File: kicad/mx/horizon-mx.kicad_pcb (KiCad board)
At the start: 2 copper layers, 266 x 76 mm, 117 parts, among them SW1 SW_Push, SW10 SW_Push, SW11 SW_Push, SW12 SW_Push, SW13 SW_Push, SW14 SW_Push, SW15 SW_Push, SW16 SW_Push, SW17 SW_Push, SW18 SW_Push, SW19 SW_Push, SW2 SW_Push, SW20 SW_Push, SW21 SW_Push, SW22 SW_Push, SW23 SW_Push, SW24 SW_Push, SW25 SW_Push, SW26 SW_Push, SW27 SW_Push, SW28 SW_Push, SW29 SW_Push, SW3 SW_Push, SW30 SW_Push, SW31 SW_Push, SW32 SW_Push, SW33 SW_Push, SW34 SW_Push, SW35 SW_Push, SW36 SW_Push, SW37 SW_Push, SW38 SW_Push, SW39 SW_Push, SW4 SW_Push, SW40 SW_Push, SW41 SW_Push, SW42 SW_Push, SW43 SW_Push, SW44 SW_Push, SW45 SW_Push, SW46 SW_Push, SW47 SW_Push, SW48 SW_Push, SW49 SW_Push, SW5 SW_Push, SW50 SW_Push, SW51 SW_Push, SW52 SW_Push, SW6 SW_Push, SW7 SW_Push, SW8 SW_Push, SW9 SW_Push, U1 PRO-MICRO

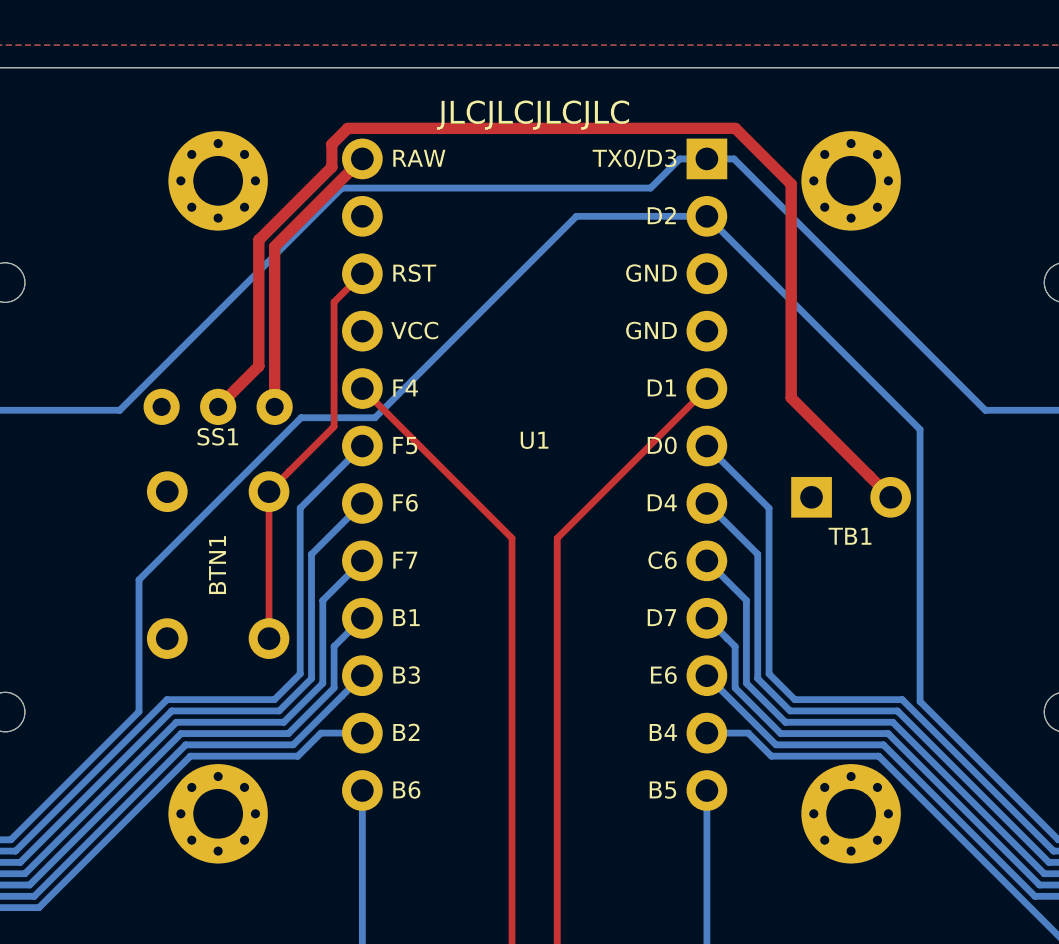
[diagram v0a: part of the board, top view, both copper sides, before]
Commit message: Clean up plate cuts, update MX board with battery removed
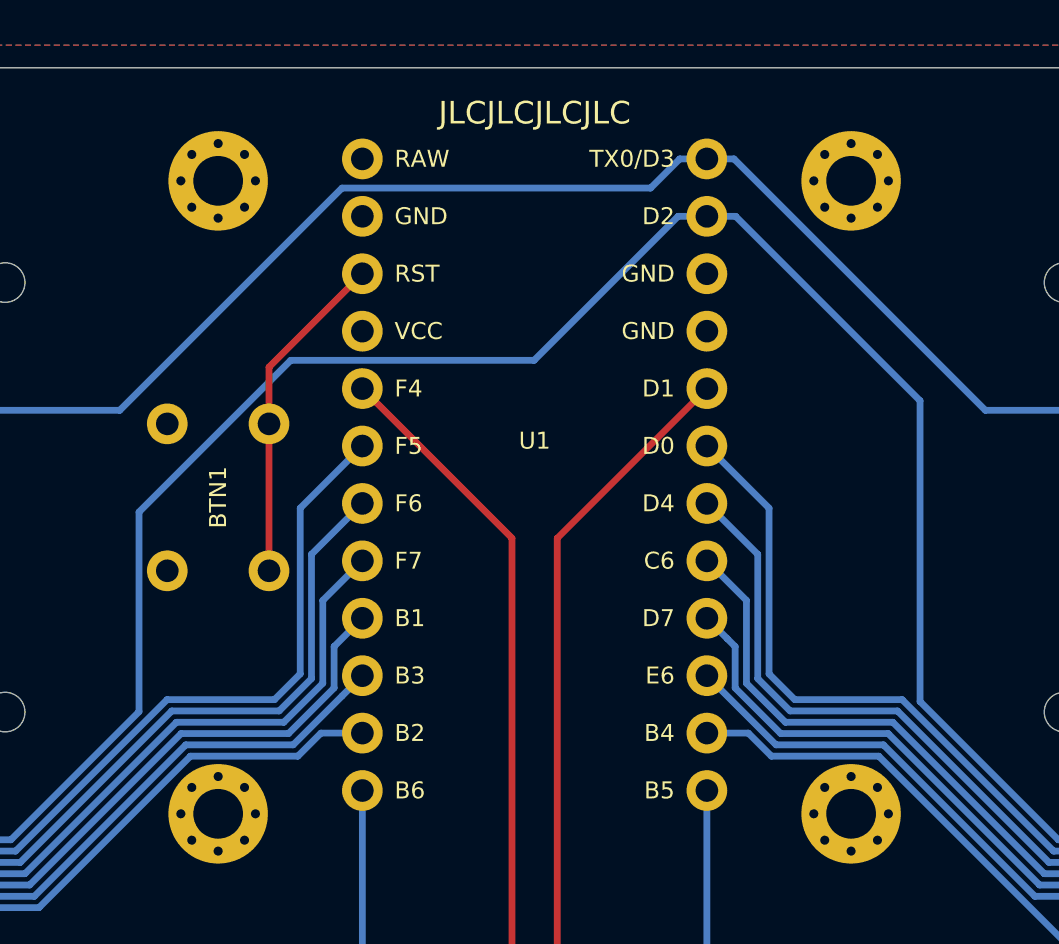
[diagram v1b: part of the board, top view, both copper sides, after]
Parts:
- removed SS1: POWER, horizon-footprints:SS12D00
- removed TB1: BATTERY, horizon-footprints:KF350-2P
- moved BTN1 3.00 mm to (195.0, 114.0)
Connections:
- U1 pad 24: RAW -> (no net)
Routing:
- net +BATT: track 51.0 -> 0.00 mm
- net RAW: track 12.6 -> 0.00 mm
- net RESET: track 17.9 -> 14.9 mm
- net ROW2: track 302.0 -> 304.5 mm

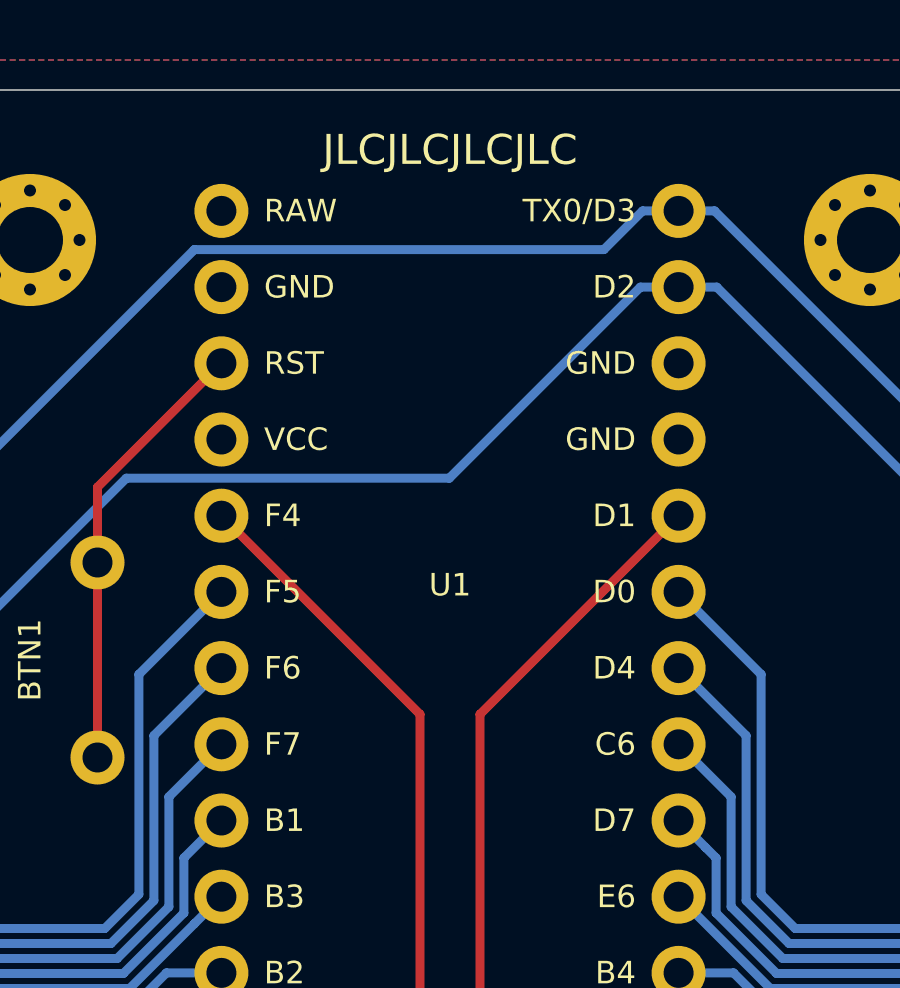
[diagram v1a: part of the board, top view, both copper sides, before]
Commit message: Preserve logos on plate PCBs
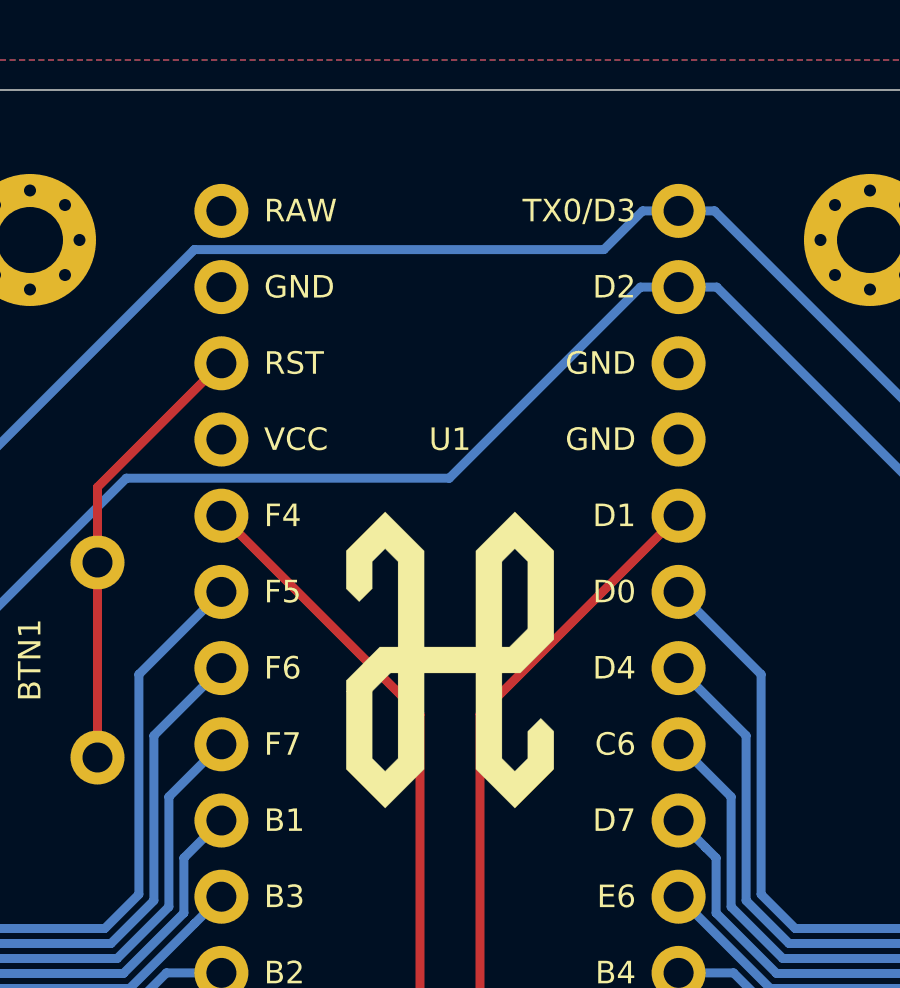
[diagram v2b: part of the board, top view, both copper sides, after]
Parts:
- added LOGO2: Logo-Top, horizon-footprints:Logo_Horizon_H, F.Cu at (209.0, 114.0)
- LOGO1: value Logo -> Logo-Bottom
- moved LOGO1 23.0 mm to (209.0, 100.5)
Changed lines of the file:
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@@
     (tracks 394)
     (zones 0)
-    (modules 115)
+    (modules 116)
     (nets 81)
   )
@@
     (add_net GND)
   )
+  (module horizon-footprints:Logo_Horizon_H (layer F.Cu)
+    (at 209 114)
+    (fp_text reference LOGO2 (at 0 2) (layer F.SilkS) hide
+      (effects (font (size 1.524 1.524) (thickness 0.3)))
+    )
+    (fp_text value Logo-Top (at 0 -2) (layer F.SilkS) hide
+      (effects (font (size 1.524 1.524) (thickness 0.3)))
+    )
+    (fp_poly (pts (xy 2.811161 -4.287795) (xy 3.459892 -3.639066) (xy 3.459892 -0.685799) (xy 2.900748 -0.126656)
+      (xy 2.341604 0.432486) (xy 1.731319 0.432486) (xy 1.731319 3.280722) (xy 1.94722 3.49662)
+      (xy 2.163122 3.712519) (xy 2.37902 3.496617) (xy 2.594919 3.280715) (xy 2.594919 2.378679)
+      (xy 2.810817 2.162777) (xy 2.83116 2.14244) (xy 2.850995 2.122623) (xy 2.870235 2.103411)
+      (xy 2.888793 2.084893) (xy 2.906579 2.067156) (xy 2.923508 2.050287) (xy 2.93949 2.034374)
+      (xy 2.954438 2.019503) (xy 2.968264 2.005761) (xy 2.980881 1.993237) (xy 2.9922 1.982017)
+      (xy 3.002134 1.972189) (xy 3.010594 1.96384) (xy 3.017494 1.957056) (xy 3.022745 1.951926)
+      (xy 3.02626 1.948537) (xy 3.02795 1.946975) (xy 3.028092 1.946875) (xy 3.029178 1.947832)
+      (xy 3.032118 1.950645) (xy 3.036821 1.955226) (xy 3.043201 1.961488) (xy 3.051169 1.969343)
+      (xy 3.060638 1.978705) (xy 3.07152 1.989485) (xy 3.083726 2.001596) (xy 3.097169 2.014952)
+      (xy 3.111761 2.029464) (xy 3.127413 2.045045) (xy 3.144038 2.061608) (xy 3.161548 2.079065)
+      (xy 3.179855 2.097329) (xy 3.198872 2.116313) (xy 3.218509 2.135929) (xy 3.238679 2.15609)
+      (xy 3.24468 2.162091) (xy 3.459892 2.377306) (xy 3.459892 3.639066) (xy 2.16243 4.936524)
+      (xy 1.513702 4.287791) (xy 0.864973 3.639058) (xy 0.864973 0.432486) (xy -0.8636 0.432486)
+      (xy -0.8636 3.639058) (xy -1.511985 4.287448) (xy -1.547393 4.322855) (xy -1.582321 4.357781)
+      (xy -1.616719 4.392174) (xy -1.650537 4.425985) (xy -1.683724 4.459163) (xy -1.716229 4.491659)
+      (xy -1.748003 4.52342) (xy -1.778995 4.554399) (xy -1.809155 4.584543) (xy -1.838431 4.613803)
+      (xy -1.866775 4.642128) (xy -1.894136 4.669469) (xy -1.920462 4.695774) (xy -1.945705 4.720994)
+      (xy -1.969813 4.745078) (xy -1.992736 4.767976) (xy -2.014425 4.789637) (xy -2.034827 4.810012)
+      (xy -2.053894 4.82905) (xy -2.071574 4.8467) (xy -2.087818 4.862913) (xy -2.102575 4.877638)
+      (xy -2.115795 4.890825) (xy -2.127427 4.902423) (xy -2.13742 4.912383) (xy -2.145726 4.920653)
+      (xy -2.152293 4.927184) (xy -2.15707 4.931925) (xy -2.160008 4.934826) (xy -2.161057 4.935837)
+      (xy -2.161058 4.935838) (xy -2.162058 4.934875) (xy -2.16495 4.932021) (xy -2.169682 4.927325)
+      (xy -2.176204 4.920839) (xy -2.184467 4.912612) (xy -2.194419 4.902694) (xy -2.20601 4.891136)
+      (xy -2.21919 4.877989) (xy -2.233909 4.863302) (xy -2.250116 4.847126) (xy -2.267761 4.829511)
+      (xy -2.286794 4.810508) (xy -2.307164 4.790166) (xy -2.32882 4.768536) (xy -2.351713 4.745669)
+      (xy -2.375792 4.721614) (xy -2.401007 4.696422) (xy -2.427307 4.670144) (xy -2.454642 4.642829)
+      (xy -2.482962 4.614527) (xy -2.512216 4.585291) (xy -2.542354 4.555168) (xy -2.573326 4.52421)
+      (xy -2.605081 4.492468) (xy -2.637569 4.45999) (xy -2.670739 4.426829) (xy -2.704541 4.393033)
+      (xy -2.738926 4.358654) (xy -2.773842 4.323741) (xy -2.810133 4.28745) (xy -3.458519 3.639063)
+      (xy -3.458519 1.044143) (xy -2.593546 1.044143) (xy -2.593546 3.280715) (xy -2.377648 3.496617)
+      (xy -2.161749 3.712519) (xy -1.945848 3.49662) (xy -1.729946 3.280722) (xy -1.729946 0.432486)
+      (xy -1.981884 0.432486) (xy -2.287715 0.738315) (xy -2.593546 1.044143) (xy -3.458519 1.044143)
+      (xy -3.458519 0.685798) (xy -2.899375 0.126656) (xy -2.340231 -0.432487) (xy -1.729946 -0.432487)
+      (xy -1.729946 -3.280722) (xy -1.945848 -3.496621) (xy -2.161749 -3.712519) (xy -2.377648 -3.496618)
+      (xy -2.593546 -3.280716) (xy -2.593546 -2.378679) (xy -2.809445 -2.162778) (xy -2.829787 -2.142441)
+      (xy -2.849622 -2.122623) (xy -2.868863 -2.103412) (xy -2.88742 -2.084894) (xy -2.905207 -2.067157)
+      (xy -2.922135 -2.050288) (xy -2.938117 -2.034374) (xy -2.953065 -2.019503) (xy -2.966892 -2.005762)
+      (xy -2.979508 -1.993238) (xy -2.990827 -1.982018) (xy -3.000761 -1.97219) (xy -3.009222 -1.96384)
+      (xy -3.016122 -1.957057) (xy -3.021373 -1.951927) (xy -3.024887 -1.948537) (xy -3.026578 -1.946975)
+      (xy -3.026719 -1.946876) (xy -3.027806 -1.947833) (xy -3.030745 -1.950646) (xy -3.035449 -1.955227)
+      (xy -3.041829 -1.961488) (xy -3.049797 -1.969344) (xy -3.059266 -1.978705) (xy -3.070147 -1.989485)
+      (xy -3.082354 -2.001597) (xy -3.095797 -2.014952) (xy -3.110388 -2.029464) (xy -3.126041 -2.045045)
+      (xy -3.142666 -2.061608) (xy -3.160176 -2.079066) (xy -3.178483 -2.09733) (xy -3.197499 -2.116314)
+      (xy -3.217136 -2.13593) (xy -3.237306 -2.156091) (xy -3.243307 -2.162091) (xy -3.458519 -2.377306)
+      (xy -3.458519 -3.639066) (xy -2.809789 -4.287795) (xy -2.161058 -4.936525) (xy -0.8636 -3.639059)
+      (xy -0.8636 -0.432487) (xy 0.864973 -0.432487) (xy 0.864973 -3.280716) (xy 1.731319 -3.280716)
+      (xy 1.731319 -0.432487) (xy 1.983257 -0.432487) (xy 2.289088 -0.738315) (xy 2.594919 -1.044144)
+      (xy 2.594919 -3.280722) (xy 2.379017 -3.496621) (xy 2.163115 -3.712519) (xy 1.947217 -3.496618)
+      (xy 1.731319 -3.280716) (xy 0.864973 -3.280716) (xy 0.864973 -3.639059) (xy 1.513702 -4.287792)
+      (xy 2.16243 -4.936525) (xy 2.811161 -4.287795)) (layer F.SilkS) (width 0.01))
+  )
   (module horizon-footprints:SW_Push_6mm (layer F.Cu)
     (at 195 114 270)
@@
   )
   (module horizon-footprints:Logo_Horizon_Small (layer B.Cu)
-    (at 209 123.5 180)
-    (fp_text reference LOGO1 (at 0 0) (layer B.SilkS) hide
+    (at 209 100.5 180)
+    (fp_text reference LOGO1 (at 0 -2) (layer B.SilkS) hide
       (effects (font (size 1.524 1.524) (thickness 0.3)) (justify mirror))
     )
-    (fp_text value Logo (at 0.75 0) (layer B.SilkS) hide
+    (fp_text value Logo-Bottom (at -0.1 1) (layer B.SilkS) hide
       (effects (font (size 1.524 1.524) (thickness 0.3)) (justify mirror))
     )
@@
     (descr "SparkFun Arduino Pro Micro ATmega32U4")
     (tags "Arduino, Pro Micro")
-    (fp_text reference U1 (at 0 16.5) (layer F.SilkS)
+    (fp_text reference U1 (at 0 11.65) (layer F.SilkS)
       (effects (font (size 0.75 0.75) (thickness 0.15)))
     )
-    (fp_text value PRO-MICRO (at 0 18) (layer F.SilkS) hide
+    (fp_text value PRO-MICRO (at 0 13.65) (layer F.SilkS) hide
       (effects (font (size 0.75 0.75) (thickness 0.15)))
     )
@@
   (gr_line (start 342 97) (end 342 169) (layer B.Adhes) (width 0.05))
   (gr_line (start 78 95) (end 340 95) (layer B.Adhes) (width 0.05))
-  (gr_text github.com/skarrmann/horizon (at 209 129.5) (layer B.SilkS)
+  (gr_text github.com/skarrmann/horizon (at 209 96.5) (layer B.SilkS)
     (effects (font (size 1 1) (thickness 0.15)) (justify mirror))
   )
-  (gr_text "rev2 | MX" (at 209 127.5) (layer B.SilkS)
+  (gr_text "rev2 | MX" (at 209 104.5) (layer B.SilkS)
     (effects (font (size 1 1) (thickness 0.15)) (justify mirror))
   )
   (gr_arc (start 78 169) (end 76 169) (angle -90) (layer Edge.Cuts) (width 0.05))
   (gr_arc (start 340 169) (end 340 171) (angle -90) (layer Edge.Cuts) (width 0.05))
-  (gr_text JLCJLCJLCJLC (at 209 97) (layer F.SilkS)
-    (effects (font (size 1 1) (thickness 0.15)))
+  (gr_text JLCJLCJLCJLC (at 209 106.5) (layer B.SilkS)
+    (effects (font (size 1 1) (thickness 0.15)) (justify mirror))
   )
   (gr_arc (start 340 97) (end 342 97) (angle -90) (layer Edge.Cuts) (width 0.05))

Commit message: Remove unused footprints and other files. Update readme. Prepare for production!
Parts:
- moved LOGO1 13.0 mm to (209.0, 113.5)
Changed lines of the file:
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@@
   )
   (module horizon-footprints:Logo_Horizon_Small (layer B.Cu)
-    (at 209 100.5 180)
+    (at 209 113.5 180)
     (fp_text reference LOGO1 (at 0 -2) (layer B.SilkS) hide
       (effects (font (size 1.524 1.524) (thickness 0.3)) (justify mirror))
@@
     (effects (font (size 1 1) (thickness 0.15)) (justify mirror))
   )
-  (gr_text "rev2 | MX" (at 209 104.5) (layer B.SilkS)
+  (gr_text "rev2 | MX" (at 209 117.5) (layer B.SilkS)
     (effects (font (size 1 1) (thickness 0.15)) (justify mirror))
   )
   (gr_arc (start 78 169) (end 76 169) (angle -90) (layer Edge.Cuts) (width 0.05))
   (gr_arc (start 340 169) (end 340 171) (angle -90) (layer Edge.Cuts) (width 0.05))
-  (gr_text JLCJLCJLCJLC (at 209 106.5) (layer B.SilkS)
+  (gr_text JLCJLCJLCJLC (at 209 131.5) (layer B.SilkS)
     (effects (font (size 1 1) (thickness 0.15)) (justify mirror))
   )
